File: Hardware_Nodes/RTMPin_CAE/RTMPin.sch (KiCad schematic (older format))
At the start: 150 parts, among them J2 Conn_01x06, J3 Conn_01x06, J4 Conn_01x06, J5 Conn_01x06, J6 Conn_01x06, J7 Conn_01x06, J8 Conn_01x06, J9 Conn_01x06, Q2 IRLR3410, Q3 IRLR3410, Q4 IRLR3410, Q5 IRLR3410, Q6 IRLR3410, Q7 IRLR3410, Q8 IRLR3410, Q9 IRLR3410, U2 SN74LVC14A, U3 ADM3483, U4 BlackPill STM32F4xx, U5 SN74LVC14A, U6 SN74AHCT1G125, U7 SN74LVC14A

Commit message: HW bugfix
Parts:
- C1, C11, C12, C13, C14, C19, C2, C20, C21, C22, C23, C25, C26, C27, C3, C31, C33, C34, C35, C36, C37, C38, C39, C40, C7, C8, C9: footprint Capacitor_SMD:C_0603_1608Metric_Pad1.08x0.95mm_HandSolder -> Capacitor_SMD:C_0603_1608Metric
- C10, C15, C16, C17, C18, C28, C29, C30, C4, C5, C6: footprint Capacitor_SMD:C_1206_3216Metric_Pad1.33x1.80mm_HandSolder -> Capacitor_SMD:C_1206_3216Metric
- D10, D11, D15, D16, D17, D18, D19, D20, D24, D25, D27, D28, D29, D30, D5, D6, D7, D8, D9: footprint Diode_SMD:D_SOD-323_HandSoldering -> Diode_SMD:D_SOD-323
- R1, R10, R11, R12, R13, R14, R15, R16, R17, R18, R19, R2, R20, R21, R22, R23, R24, R25, R26, R27, R28, R29, R3, R30, R31, R32, R33, R35, R36, R37, R38, R39, R4, R40, R41, R42, R43, R44, R45, R46, R47, R48, R49, R5, R50, R51, R52, R53, R54, R55, R56, R57, R58, R6, R7, R8, R9: footprint Resistor_SMD:R_0603_1608Metric_Pad0.98x0.95mm_HandSolder -> Resistor_SMD:R_0603_1608Metric
- U6: footprint Package_TO_SOT_SMD:SOT-23-5_HandSoldering -> Package_TO_SOT_SMD:SOT-23-5
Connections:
- wire segments 471 -> 474
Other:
- moved on the sheet: R21

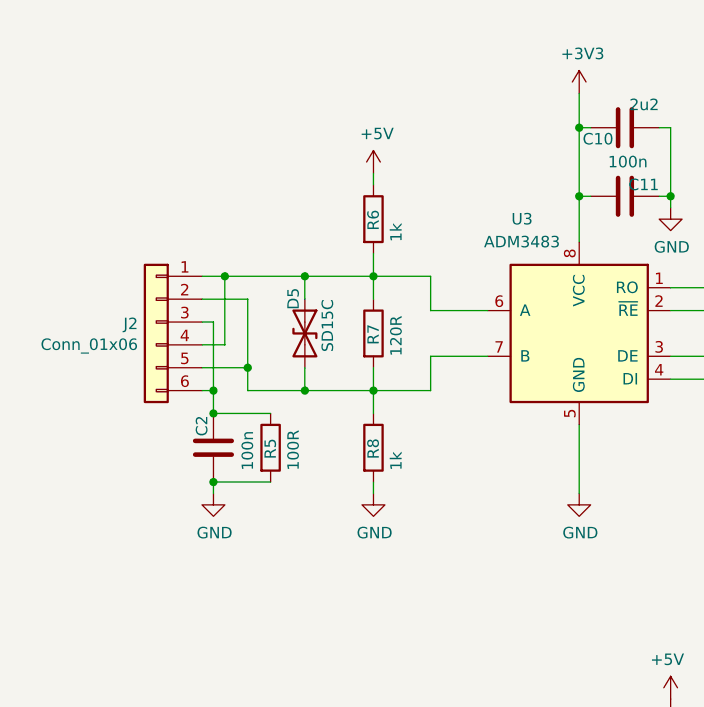
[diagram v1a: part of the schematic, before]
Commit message: all parts on top side
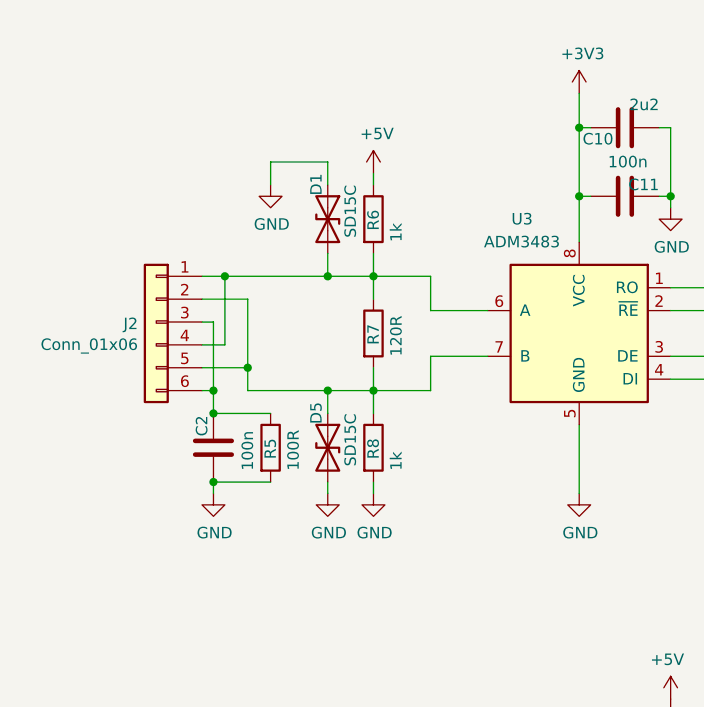
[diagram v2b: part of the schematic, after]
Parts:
- added D1: SD15C, Diode_SMD:D_SOD-323, symbol Device:D_TVS
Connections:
- wire segments 474 -> 478
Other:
- moved on the sheet: D5
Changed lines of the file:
@@
 L Device:D_TVS D5
 U 1 1 6142DABA
-P 2000 2450
-F 0 "D5" H 1800 2400 50  0000 L CNN
-F 1 "SD15C" H 1850 2550 50  0000 L CNN
-F 2 "Diode_SMD:D_SOD-323" H 2000 2450 50  0001 C CNN
-F 3 "~" H 2000 2450 50  0001 C CNN
-	1    2000 2450
+P 2100 2950
+F 0 "D5" H 1900 2900 50  0000 L CNN
+F 1 "SD15C" H 1950 3050 50  0000 L CNN
+F 2 "Diode_SMD:D_SOD-323" H 2100 2950 50  0001 C CNN
+F 3 "~" H 2100 2950 50  0001 C CNN
+	1    2100 2950
 	0    1    1    0
 $EndComp
@@
 	1750 2300 1750 2600
 Wire Wire Line
-	1750 2700 2000 2700
-Wire Wire Line
 	2550 2700 2550 2550
 Wire Wire Line
@@
 Wire Wire Line
 	1550 2300 1750 2300
-Wire Wire Line
-	2000 2300 2000 2200
-Connection ~ 2000 2200
-Wire Wire Line
-	2000 2200 2300 2200
-Wire Wire Line
-	2000 2600 2000 2700
-Connection ~ 2000 2700
-Wire Wire Line
-	2000 2700 2300 2700
 $Comp
 L Device:C C11
@@
 Connection ~ 1650 2200
 Wire Wire Line
-	1650 2200 2000 2200
-Wire Wire Line
 	1550 2600 1750 2600
 Connection ~ 1750 2600
@@
 	4350 2250 4350 2650
 $Comp
-L power:GND #PWR?
+L power:GND #PWR012
 U 1 1 6360935A
 P 3900 3150
-F 0 "#PWR?" H 3900 2900 50  0001 C CNN
+F 0 "#PWR012" H 3900 2900 50  0001 C CNN
 F 1 "GND" H 3905 2977 50  0000 C CNN
 F 2 "" H 3900 3150 50  0001 C CNN
@@
 Wire Wire Line
 	3900 3050 3900 3150
+$Comp
+L Device:D_TVS D1
+U 1 1 633DAF07
+P 2100 1950
+F 0 "D1" H 1900 1900 50  0000 L CNN
+F 1 "SD15C" H 1950 2050 50  0000 L CNN
+F 2 "Diode_SMD:D_SOD-323" H 2100 1950 50  0001 C CNN
+F 3 "~" H 2100 1950 50  0001 C CNN
+	1    2100 1950
+	0    1    1    0
+$EndComp
+Wire Wire Line
+	1650 2200 2100 2200
+Wire Wire Line
+	1750 2700 2100 2700
+Wire Wire Line
+	2100 2800 2100 2700
+Connection ~ 2100 2700
+Wire Wire Line
+	2100 2700 2300 2700
+Wire Wire Line
+	2100 2100 2100 2200
+Connection ~ 2100 2200
+Wire Wire Line
+	2100 2200 2300 2200
+$Comp
+L power:GND #PWR011
+U 1 1 634E6FDE
+P 2100 3150
+F 0 "#PWR011" H 2100 2900 50  0001 C CNN
+F 1 "GND" H 2105 2977 50  0000 C CNN
+F 2 "" H 2100 3150 50  0001 C CNN
+F 3 "" H 2100 3150 50  0001 C CNN
+	1    2100 3150
+	1    0    0    -1
+$EndComp
+$Comp
+L power:GND #PWR01
+U 1 1 63526EA0
+P 1850 1800
+F 0 "#PWR01" H 1850 1550 50  0001 C CNN
+F 1 "GND" H 1855 1627 50  0000 C CNN
+F 2 "" H 1850 1800 50  0001 C CNN
+F 3 "" H 1850 1800 50  0001 C CNN
+	1    1850 1800
+	1    0    0    -1
+$EndComp
+Wire Wire Line
+	2100 1800 2100 1700
+Wire Wire Line
+	2100 1700 1850 1700
+Wire Wire Line
+	1850 1700 1850 1800
+Wire Wire Line
+	2100 3100 2100 3150
 $EndSCHEMATC

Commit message: tvs unipolar
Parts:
- C10: value 2u2 -> 10u 25V
- D1, D5: value SD15C -> SD15; symbol Device:D_TVS -> Device:D_Zener
- D10, D11, D15, D16, D17, D18, D19, D20, D24, D25, D27, D28, D29, D30, D6, D7, D8, D9: value SD15C -> SD05; symbol Device:D_TVS -> Device:D_Zener
- D26: value SMAJ48CA -> SMAJ48; symbol Device:D_TVS -> Device:D_Zener
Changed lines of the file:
@@
 	9200 1550 8950 1550
 $Comp
-L Device:D_TVS D26
+L Device:D_Zener D26
 U 1 1 6144B176
 P 11650 8850
 F 0 "D26" H 11450 8800 50  0000 L CNN
-F 1 "SMAJ48CA" H 11400 8950 50  0000 L CNN
+F 1 "SMAJ48" H 11400 8950 50  0000 L CNN
 F 2 "Diode_SMD:D_SMA" H 11650 8850 50  0001 C CNN
 F 3 "~" H 11650 8850 50  0001 C CNN
@@
 $EndComp
 $Comp
-L Device:D_TVS D5
-U 1 1 6142DABA
-P 2100 2950
-F 0 "D5" H 1900 2900 50  0000 L CNN
-F 1 "SD15C" H 1950 3050 50  0000 L CNN
-F 2 "Diode_SMD:D_SOD-323" H 2100 2950 50  0001 C CNN
-F 3 "~" H 2100 2950 50  0001 C CNN
-	1    2100 2950
-	0    1    1    0
-$EndComp
-$Comp
 L Device:R R6
 U 1 1 61430167
@@
 Connection ~ 11900 5750
 $Comp
-L Device:D_TVS D24
+L Device:D_Zener D24
 U 1 1 615DA327
 P 9200 1300
 F 0 "D24" H 9000 1250 50  0000 L CNN
-F 1 "SD15C" H 9050 1400 50  0000 L CNN
+F 1 "SD05" H 9050 1400 50  0000 L CNN
 F 2 "Diode_SMD:D_SOD-323" H 9200 1300 50  0001 C CNN
 F 3 "~" H 9200 1300 50  0001 C CNN
@@
 $EndComp
 $Comp
-L Device:D_TVS D25
+L Device:D_Zener D25
 U 1 1 6162DAC3
 P 9200 1850
 F 0 "D25" H 9200 1750 50  0000 L CNN
-F 1 "SD15C" H 9050 1950 50  0000 L CNN
+F 1 "SD05" H 9050 1950 50  0000 L CNN
 F 2 "Diode_SMD:D_SOD-323" H 9200 1850 50  0001 C CNN
 F 3 "~" H 9200 1850 50  0001 C CNN
@@
 	9200 1650 9750 1650
 $Comp
-L Device:D_TVS D27
+L Device:D_Zener D27
 U 1 1 617C3486
 P 12400 4500
 F 0 "D27" H 12400 4400 50  0000 L CNN
-F 1 "SD15C" H 12250 4600 50  0000 L CNN
+F 1 "SD05" H 12250 4600 50  0000 L CNN
 F 2 "Diode_SMD:D_SOD-323" H 12400 4500 50  0001 C CNN
 F 3 "~" H 12400 4500 50  0001 C CNN
@@
 $EndComp
 $Comp
-L Device:D_TVS D29
+L Device:D_Zener D29
 U 1 1 61810120
 P 12400 5600
 F 0 "D29" H 12400 5500 50  0000 L CNN
-F 1 "SD15C" H 12250 5700 50  0000 L CNN
+F 1 "SD05" H 12250 5700 50  0000 L CNN
 F 2 "Diode_SMD:D_SOD-323" H 12400 5600 50  0001 C CNN
 F 3 "~" H 12400 5600 50  0001 C CNN
@@
 $EndComp
 $Comp
-L Device:D_TVS D28
+L Device:D_Zener D28
 U 1 1 618D6D12
 P 12400 5050
 F 0 "D28" H 12400 4950 50  0000 L CNN
-F 1 "SD15C" H 12250 5150 50  0000 L CNN
+F 1 "SD05" H 12250 5150 50  0000 L CNN
 F 2 "Diode_SMD:D_SOD-323" H 12400 5050 50  0001 C CNN
 F 3 "~" H 12400 5050 50  0001 C CNN
@@
 	12400 4900 12050 4900
 $Comp
-L Device:D_TVS D30
+L Device:D_Zener D30
 U 1 1 6190DAEB
 P 12400 6150
 F 0 "D30" H 12400 6050 50  0000 L CNN
-F 1 "SD15C" H 12250 6250 50  0000 L CNN
+F 1 "SD05" H 12250 6250 50  0000 L CNN
 F 2 "Diode_SMD:D_SOD-323" H 12400 6150 50  0001 C CNN
 F 3 "~" H 12400 6150 50  0001 C CNN
@@
 	13100 4350 12400 4350
 $Comp
-L Device:D_TVS D15
+L Device:D_Zener D15
 U 1 1 61B42716
 P 7500 4500
 F 0 "D15" H 7500 4400 50  0000 L CNN
-F 1 "SD15C" H 7350 4600 50  0000 L CNN
+F 1 "SD05" H 7350 4600 50  0000 L CNN
 F 2 "Diode_SMD:D_SOD-323" H 7500 4500 50  0001 C CNN
 F 3 "~" H 7500 4500 50  0001 C CNN
@@
 	7500 4350 7250 4350
 $Comp
-L Device:D_TVS D16
+L Device:D_Zener D16
 U 1 1 61B8E710
 P 7500 5050
 F 0 "D16" H 7500 4950 50  0000 L CNN
-F 1 "SD15C" H 7350 5150 50  0000 L CNN
+F 1 "SD05" H 7350 5150 50  0000 L CNN
 F 2 "Diode_SMD:D_SOD-323" H 7500 5050 50  0001 C CNN
 F 3 "~" H 7500 5050 50  0001 C CNN
@@
 	7500 4900 7350 4900
 $Comp
-L Device:D_TVS D17
+L Device:D_Zener D17
 U 1 1 61BCDA86
 P 7500 5600
 F 0 "D17" H 7500 5500 50  0000 L CNN
-F 1 "SD15C" H 7350 5700 50  0000 L CNN
+F 1 "SD05" H 7350 5700 50  0000 L CNN
 F 2 "Diode_SMD:D_SOD-323" H 7500 5600 50  0001 C CNN
 F 3 "~" H 7500 5600 50  0001 C CNN
@@
 	7500 5450 6650 5450
 $Comp
-L Device:D_TVS D18
+L Device:D_Zener D18
 U 1 1 61C1024D
 P 7500 6150
 F 0 "D18" H 7500 6050 50  0000 L CNN
-F 1 "SD15C" H 7350 6250 50  0000 L CNN
+F 1 "SD05" H 7350 6250 50  0000 L CNN
 F 2 "Diode_SMD:D_SOD-323" H 7500 6150 50  0001 C CNN
 F 3 "~" H 7500 6150 50  0001 C CNN
@@
 	7500 6000 7350 6000
 $Comp
-L Device:D_TVS D19
+L Device:D_Zener D19
 U 1 1 61C4F8C6
 P 7500 6700
 F 0 "D19" H 7500 6600 50  0000 L CNN
-F 1 "SD15C" H 9300 9000 50  0000 L CNN
+F 1 "SD05" H 9300 9000 50  0000 L CNN
 F 2 "Diode_SMD:D_SOD-323" H 7500 6700 50  0001 C CNN
 F 3 "~" H 7500 6700 50  0001 C CNN
@@
 	7500 6550 7250 6550
 $Comp
-L Device:D_TVS D20
+L Device:D_Zener D20
 U 1 1 61C8C598
 P 7500 7250
 F 0 "D20" H 7500 7150 50  0000 L CNN
-F 1 "SD15C" H 7350 7350 50  0000 L CNN
+F 1 "SD05" H 7350 7350 50  0000 L CNN
 F 2 "Diode_SMD:D_SOD-323" H 7500 7250 50  0001 C CNN
 F 3 "~" H 7500 7250 50  0001 C CNN
@@
 	7500 7100 7150 7100
 $Comp
-L Device:D_TVS D7
+L Device:D_Zener D7
 U 1 1 61E71D06
 P 2400 5050
 F 0 "D7" H 2400 4950 50  0000 L CNN
-F 1 "SD15C" H 2250 5150 50  0000 L CNN
+F 1 "SD05" H 2250 5150 50  0000 L CNN
 F 2 "Diode_SMD:D_SOD-323" H 2400 5050 50  0001 C CNN
 F 3 "~" H 2400 5050 50  0001 C CNN
@@
 	2400 4900 2250 4900
 $Comp
-L Device:D_TVS D6
+L Device:D_Zener D6
 U 1 1 61F23AAD
 P 2400 4500
 F 0 "D6" H 2400 4400 50  0000 L CNN
-F 1 "SD15C" H 2250 4600 50  0000 L CNN
+F 1 "SD05" H 2250 4600 50  0000 L CNN
 F 2 "Diode_SMD:D_SOD-323" H 2400 4500 50  0001 C CNN
 F 3 "~" H 2400 4500 50  0001 C CNN
@@
 	2400 4350 2150 4350
 $Comp
-L Device:D_TVS D8
+L Device:D_Zener D8
 U 1 1 61F67843
 P 2400 5600
 F 0 "D8" H 2400 5500 50  0000 L CNN
-F 1 "SD15C" H 2250 5700 50  0000 L CNN
+F 1 "SD05" H 2250 5700 50  0000 L CNN
 F 2 "Diode_SMD:D_SOD-323" H 2400 5600 50  0001 C CNN
 F 3 "~" H 2400 5600 50  0001 C CNN
@@
 	2400 5450 1550 5450
 $Comp
-L Device:D_TVS D9
+L Device:D_Zener D9
 U 1 1 61FB0A7A
 P 2400 6150
 F 0 "D9" H 2400 6050 50  0000 L CNN
-F 1 "SD15C" H 2250 6250 50  0000 L CNN
+F 1 "SD05" H 2250 6250 50  0000 L CNN
 F 2 "Diode_SMD:D_SOD-323" H 2400 6150 50  0001 C CNN
 F 3 "~" H 2400 6150 50  0001 C CNN
@@
 	2400 6000 2250 6000
 $Comp
-L Device:D_TVS D10
+L Device:D_Zener D10
 U 1 1 61FF2E71
 P 2400 6700
 F 0 "D10" H 2400 6600 50  0000 L CNN
-F 1 "SD15C" H 2250 6800 50  0000 L CNN
+F 1 "SD05" H 2250 6800 50  0000 L CNN
 F 2 "Diode_SMD:D_SOD-323" H 2400 6700 50  0001 C CNN
 F 3 "~" H 2400 6700 50  0001 C CNN
@@
 	2400 6550 2150 6550
 $Comp
-L Device:D_TVS D11
+L Device:D_Zener D11
 U 1 1 62038DA1
 P 2400 7250
 F 0 "D11" H 2400 7150 50  0000 L CNN
-F 1 "SD15C" H 2250 7350 50  0000 L CNN
+F 1 "SD05" H 2250 7350 50  0000 L CNN
 F 2 "Diode_SMD:D_SOD-323" H 2400 7250 50  0001 C CNN
 F 3 "~" H 2400 7250 50  0001 C CNN
@@
 P 3400 1550
 F 0 "C10" V 3350 1600 50  0000 L CNN
-F 1 "2u2" V 3500 1400 50  0000 L CNN
+F 1 "10u 25V" V 3500 1400 50  0000 L CNN
 F 2 "Capacitor_SMD:C_1206_3216Metric" H 3438 1400 50  0001 C CNN
 F 3 "~" H 3400 1550 50  0001 C CNN
@@
 Wire Wire Line
 	3900 3050 3900 3150
-$Comp
-L Device:D_TVS D1
-U 1 1 633DAF07
-P 2100 1950
-F 0 "D1" H 1900 1900 50  0000 L CNN
-F 1 "SD15C" H 1950 2050 50  0000 L CNN
-F 2 "Diode_SMD:D_SOD-323" H 2100 1950 50  0001 C CNN
-F 3 "~" H 2100 1950 50  0001 C CNN
-	1    2100 1950
-	0    1    1    0
-$EndComp
 Wire Wire Line
 	1650 2200 2100 2200
@@
 Wire Wire Line
 	2100 3100 2100 3150
+$Comp
+L Device:D_Zener D5
+U 1 1 6142DABA
+P 2100 2950
+F 0 "D5" H 1900 2900 50  0000 L CNN
+F 1 "SD15" H 1950 3050 50  0000 L CNN
+F 2 "Diode_SMD:D_SOD-323" H 2100 2950 50  0001 C CNN
+F 3 "~" H 2100 2950 50  0001 C CNN
+	1    2100 2950
+	0    1    1    0
+$EndComp
+$Comp
+L Device:D_Zener D1
+U 1 1 633DAF07
+P 2100 1950
+F 0 "D1" H 1900 1900 50  0000 L CNN
+F 1 "SD15" H 1950 2050 50  0000 L CNN
+F 2 "Diode_SMD:D_SOD-323" H 2100 1950 50  0001 C CNN
+F 3 "~" H 2100 1950 50  0001 C CNN
+	1    2100 1950
+	0    -1   -1   0
+$EndComp
 $EndSCHEMATC
